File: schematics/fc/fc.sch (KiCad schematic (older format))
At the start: 36 parts

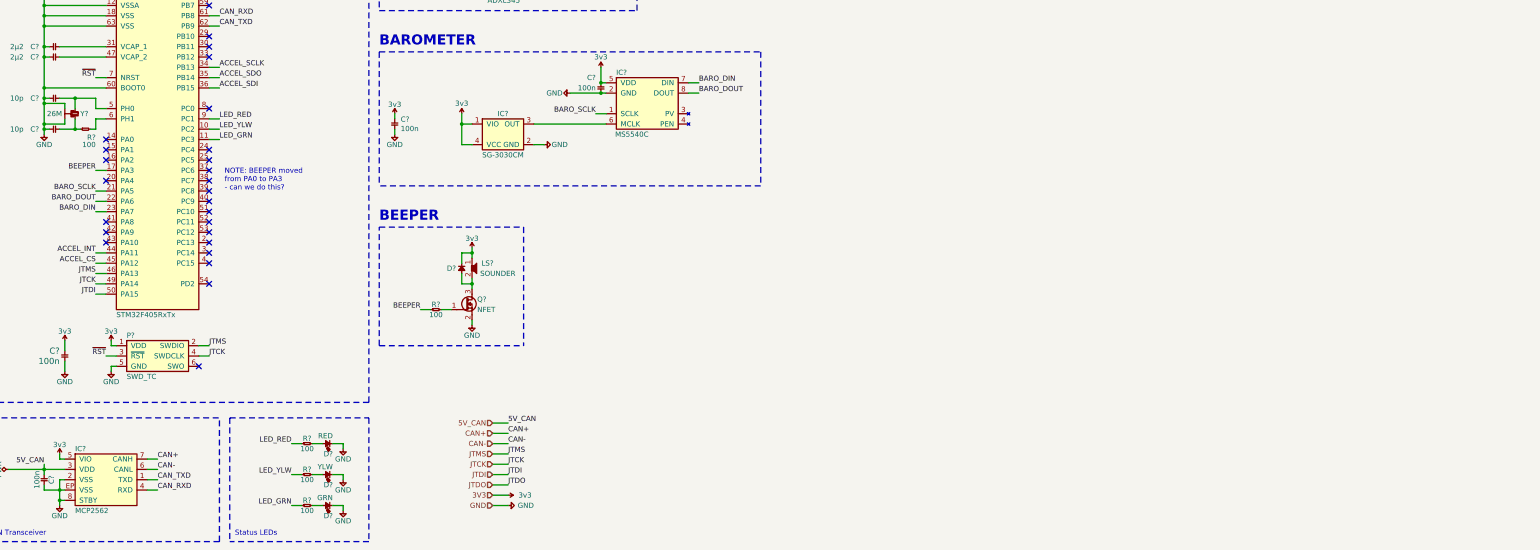
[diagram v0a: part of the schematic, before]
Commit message: Restructure into three boards
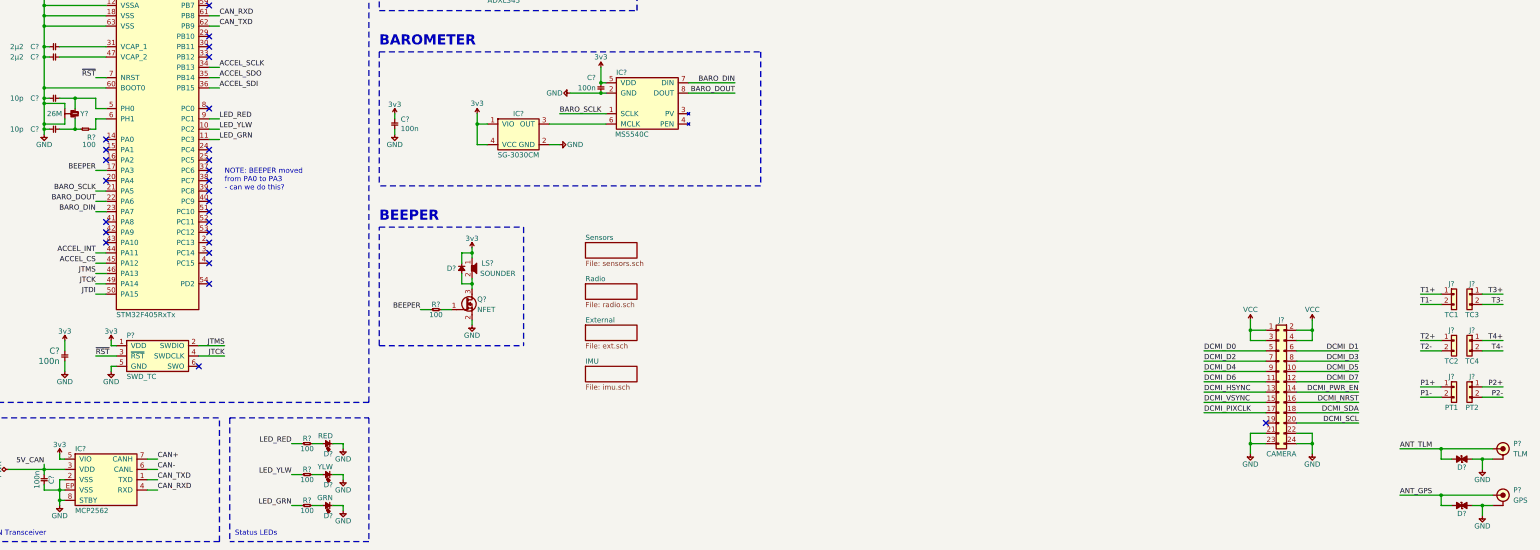
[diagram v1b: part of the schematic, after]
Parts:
- added D? (x2): ESD_DIODE, cusf:0402, symbol cusf-kicad:ESD_DIODE
- added J?: TC1, symbol cusf-kicad:CONN_01x02
- added J?: TC4, symbol cusf-kicad:CONN_01x02
- added J?: TC3, symbol cusf-kicad:CONN_01x02
- added J?: TC2, symbol cusf-kicad:CONN_01x02
- added J?: PT2, symbol cusf-kicad:CONN_01x02
- added J?: PT1, symbol cusf-kicad:CONN_01x02
- added J?: CAMERA, symbol cusf-kicad:CONN_02x12
- added P?: GPS, cusf:SMA-EDGE, symbol cusf-kicad:COAX
- added P?: TLM, cusf:SMA-EDGE, symbol cusf-kicad:COAX
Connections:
- net GND: now also D?.2, D?.2, J?.21, J?.22, J?.23, J?.24, P?.2 (GND), P?.2 (GND)
- new net ANT_GPS: D?.1, P?.1 (RF)
- new net ANT_TLM: D?.1, P?.1 (RF)
- new net DCMI_D0: J?.5
- new net DCMI_D1: J?.6
- new net DCMI_D2: J?.7
- new net DCMI_D3: J?.8
- new net DCMI_D4: J?.9
- new net DCMI_D5: J?.10
- new net DCMI_D6: J?.11
- new net DCMI_D7: J?.12
- new net DCMI_HSYNC: J?.13
- new net DCMI_NRST: J?.16
- new net DCMI_PIXCLK: J?.17
- new net DCMI_PWR_EN: J?.14
- new net DCMI_SCL: J?.20
- new net DCMI_SDA: J?.18
- new net DCMI_VSYNC: J?.15
- new net P1+: J?.1
- new net P1-: J?.2
- new net P2+: J?.1
- new net P2-: J?.2
- new net T1+: J?.1
- new net T1-: J?.2
- new net T2+: J?.1
- new net T2-: J?.2
- new net T3+: J?.1
- new net T3-: J?.2
- new net T4+: J?.1
- new net T4-: J?.2
- new net VCC: J?.1, J?.2, J?.3, J?.4
- no-connect marks 33 -> 34
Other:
- moved on the sheet: IC?
